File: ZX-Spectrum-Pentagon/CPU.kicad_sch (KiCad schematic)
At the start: 17 parts, among them U2 74HC14, U24 74HC245, U25 74HC541, U26 74HC541, U27 Z80CPU, U28 74HC244, U29 GAL16V8, U30 29F040, U31 74HC32, U8 74HC00

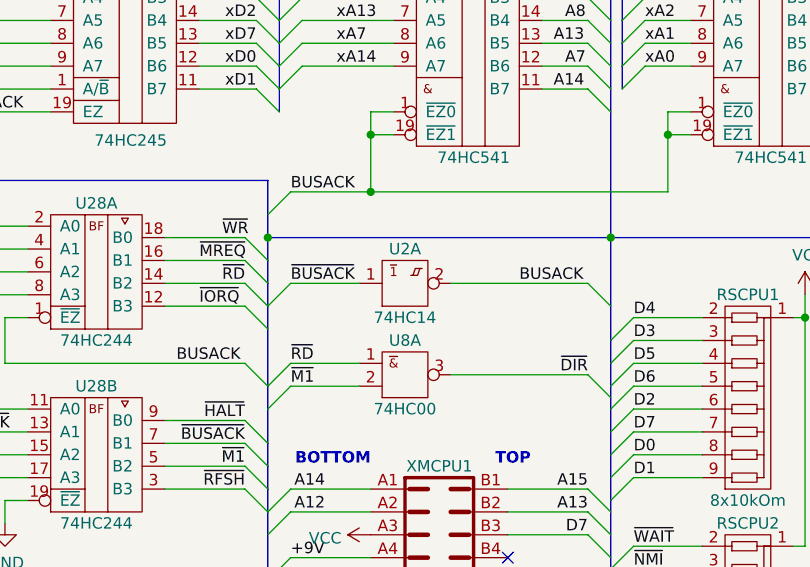
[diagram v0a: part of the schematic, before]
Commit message: delete unuser labels fix problem with units
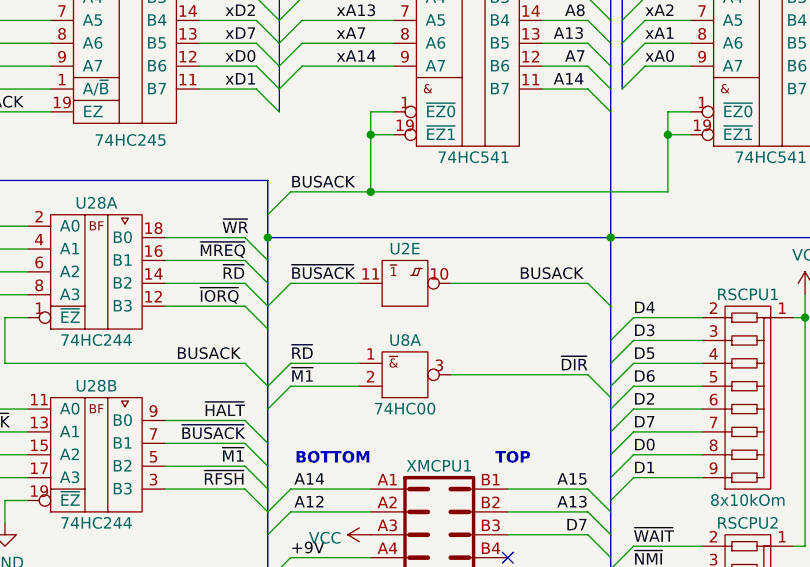
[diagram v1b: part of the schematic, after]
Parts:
- U2: value 74HC14 -> (none); footprint Package_DIP:DIP-14_W7.62mm -> (none)
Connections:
- net BUSACK: now also U2.10 (~{Y}); no longer U2.2 (~{Y})
- net ~{BUSACK}: now also U2.11 (A); no longer U2.1 (A)
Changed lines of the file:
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@@
     (pin "9")
   )
-  (symbol (lib_id "74IEC:74HC14") (at 151.13 67.31 0) (unit 1)
+  (symbol (lib_id "74IEC:74HC14") (at 151.13 67.31 0) (unit 5)
     (in_bom yes) (on_board yes)
     (property "Reference" "U2" (id 0) (at 151.13 63.5 0))
-    (property "Value" "74HC14" (id 1) (at 151.13 71.12 0))
-    (property "Footprint" "Package_DIP:DIP-14_W7.62mm" (id 2) (at 151.13 61.976 0)
+    (property "Value" "" (id 1) (at 151.13 71.12 0))
+    (property "Footprint" "" (id 2) (at 151.13 61.976 0)
       (effects (font (size 1.27 1.27)) hide)
     )

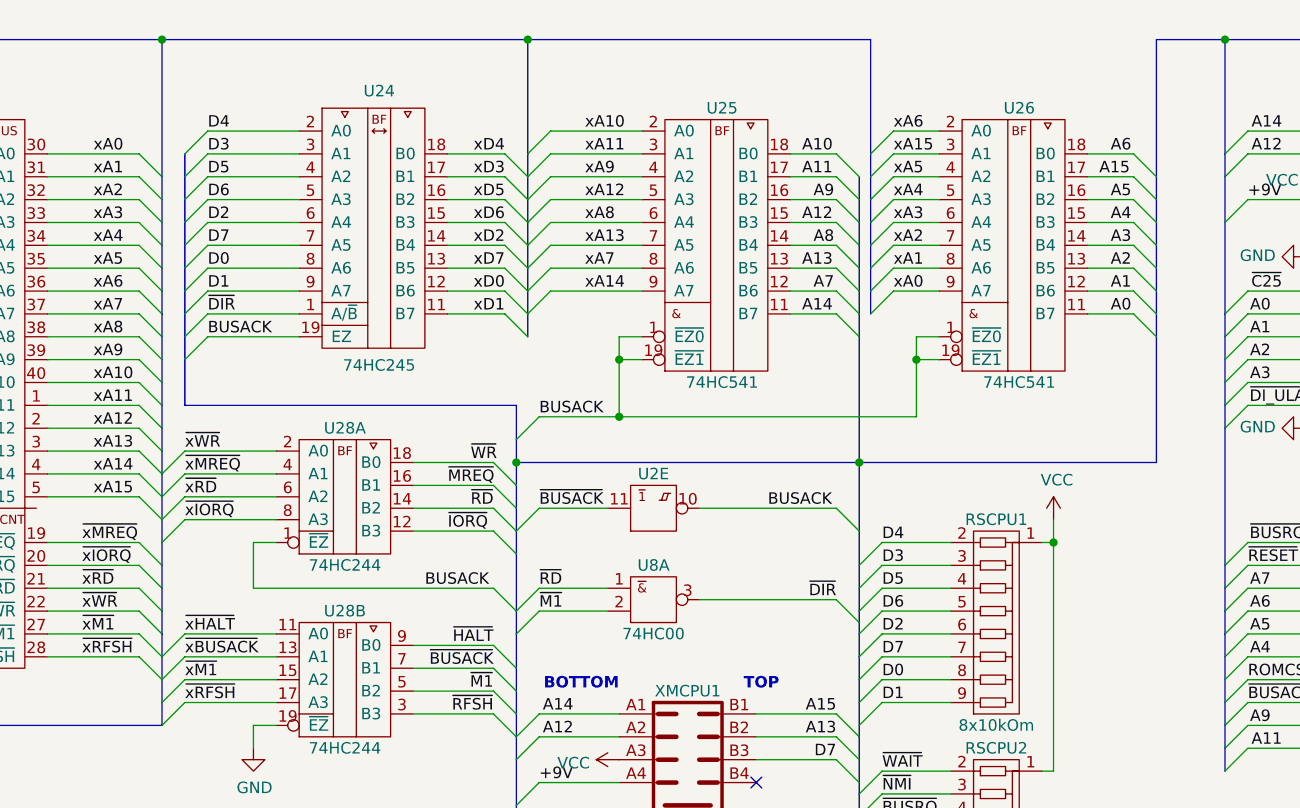
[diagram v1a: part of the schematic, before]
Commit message: chsnge some signals Make a track between CPU and buffers
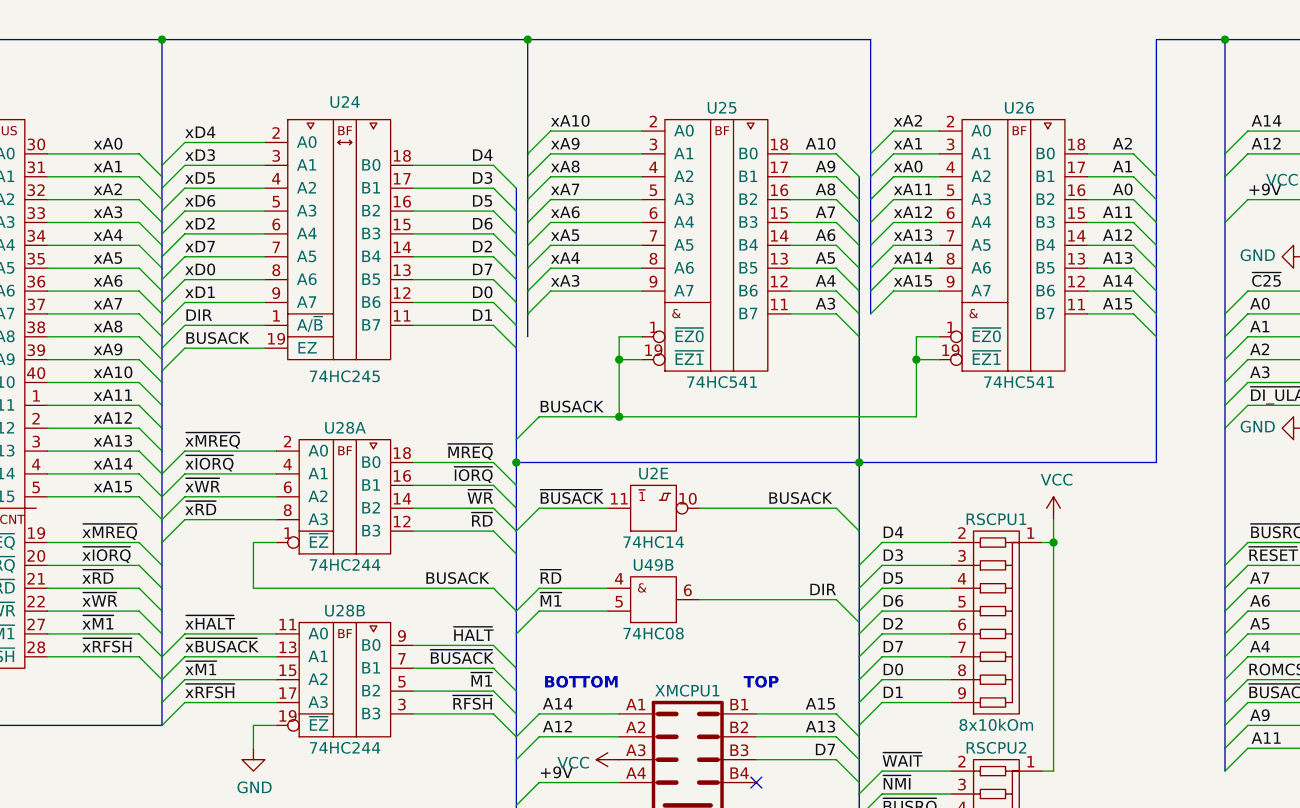
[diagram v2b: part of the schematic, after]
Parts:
- removed U8: 74HC00, Package_DIP:DIP-14_W7.62mm, symbol 74IEC:74HC00
- added U49: 74HC08, symbol 74IEC:74HC08
- U2: value (none) -> 74HC14; footprint (none) -> Package_DIP:DIP-14_W7.62mm
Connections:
- net A0: now also U26.16 (B2); no longer U26.11 (B7)
- net A1: now also U26.17 (B1); no longer U26.12 (B6)
- net A11: now also U26.15 (B3); no longer U25.17 (B1)
- net A12: now also U26.14 (B4); no longer U25.15 (B3)
- net A13: now also U26.13 (B5); no longer U25.13 (B5)
- net A14: now also U26.12 (B6); no longer U25.11 (B7)
- net A15: now also U26.11 (B7); no longer U26.17 (B1)
- net A2: now also U26.18 (B0); no longer U26.13 (B5)
- net A3: now also U25.11 (B7); no longer U26.14 (B4)
- net A4: now also U25.12 (B6); no longer U26.15 (B3)
- net A5: now also U25.13 (B5); no longer U26.16 (B2)
- net A6: now also U25.14 (B4); no longer U26.18 (B0)
- net A7: now also U25.15 (B3); no longer U25.12 (B6)
- net A8: now also U25.16 (B2); no longer U25.14 (B4)
- net A9: now also U25.17 (B1); no longer U25.16 (B2)
- net D0: now also U24.12 (B6); no longer U24.8 (A6)
- net D1: now also U24.11 (B7); no longer U24.9 (A7)
- net D2: now also U24.14 (B4); no longer U24.6 (A4)
- net D3: now also U24.17 (B1); no longer U24.3 (A1)
- net D4: now also U24.18 (B0); no longer U24.2 (A0)
- net D5: now also U24.16 (B2); no longer U24.4 (A2)
- net D6: now also U24.15 (B3); no longer U24.5 (A3)
- net D7: now also U24.13 (B5); no longer U24.7 (A5)
- net GND: now also U49.7 (GND)
- net VCC: now also U49.14 (VCC)
- net xA0: now also U26.4 (A2); no longer U26.9 (A7)
- net xA1: now also U26.3 (A1); no longer U26.8 (A6)
- net xA11: now also U26.5 (A3); no longer U25.3 (A1)
- net xA12: now also U26.6 (A4); no longer U25.5 (A3)
- net xA13: now also U26.7 (A5); no longer U25.7 (A5)
- net xA14: now also U26.8 (A6); no longer U25.9 (A7)
- net xA15: now also U26.9 (A7); no longer U26.3 (A1)
- net xA2: now also U26.2 (A0); no longer U26.7 (A5)
- net xA3: now also U25.9 (A7); no longer U26.6 (A4)
- net xA4: now also U25.8 (A6); no longer U26.5 (A3)
- net xA5: now also U25.7 (A5); no longer U26.4 (A2)
- net xA6: now also U25.6 (A4); no longer U26.2 (A0)
- net xA7: now also U25.5 (A3); no longer U25.8 (A6)
- net xA8: now also U25.4 (A2); no longer U25.6 (A4)
- net xA9: now also U25.3 (A1); no longer U25.4 (A2)
- net xD0: now also U24.8 (A6); no longer U24.12 (B6)
- net xD1: now also U24.9 (A7); no longer U24.11 (B7)
- net xD2: now also U24.6 (A4); no longer U24.14 (B4)
- net xD3: now also U24.3 (A1); no longer U24.17 (B1)
- net xD4: now also U24.2 (A0); no longer U24.18 (B0)
- net xD5: now also U24.4 (A2); no longer U24.16 (B2)
- net xD6: now also U24.5 (A3); no longer U24.15 (B3)
- net xD7: now also U24.7 (A5); no longer U24.13 (B5)
- net ~{IORQ}: now also U28.16 (B1); no longer U28.12 (B3)
- net ~{M1}: now also U49.5 (B)
- net ~{MREQ}: now also U28.18 (B0); no longer U28.16 (B1)
- net ~{RD}: now also U28.12 (B3), U49.4 (A); no longer U28.14 (B2)
- net ~{WR}: now also U28.14 (B2); no longer U28.18 (B0)
- net ~{xIORQ}: now also U28.4 (A1); no longer U28.8 (A3)
- net ~{xMREQ}: now also U28.2 (A0); no longer U28.4 (A1)
- net ~{xRD}: now also U28.8 (A3); no longer U28.6 (A2)
- net ~{xWR}: now also U28.6 (A2); no longer U28.2 (A0)
- net ~{DIR} renamed DIR
- net DIR: now also U49.6 (~{Y})
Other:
- moved on the sheet: U24

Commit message: reposition object
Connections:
- net ~{NMI}: now also RSCPU2.2 (R1); no longer RSCPU2.3 (R2)
- net ~{RST}: now also RSCPU2.3 (R2); no longer RSCPU2.5 (R4)
- net ~{WAIT}: now also RSCPU2.5 (R4); no longer RSCPU2.2 (R1)
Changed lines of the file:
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@@
     (effects (font (size 1.27 1.27)) (justify right bottom))
   )
-  (label "~{NMI}" (at 176.53 99.06 0)
+  (label "~{NMI}" (at 176.53 96.52 0)
     (effects (font (size 1.27 1.27)) (justify left bottom))
   )
@@
     (effects (font (size 1.27 1.27)) (justify left bottom))
   )
-  (label "~{RST}" (at 176.53 104.14 0)
+  (label "~{RST}" (at 176.53 99.06 0)
     (effects (font (size 1.27 1.27)) (justify left bottom))
   )
@@
     (effects (font (size 1.27 1.27)) (justify right bottom))
   )
-  (label "~{WAIT}" (at 176.53 96.52 0)
-    (effects (font (size 1.27 1.27)) (justify left bottom))
-  )
+  (label "~{WAIT}" (at 176.53 104.14 0)
+    (effects (font (size 1.27 1.27)) (justify left bottom))
+  )

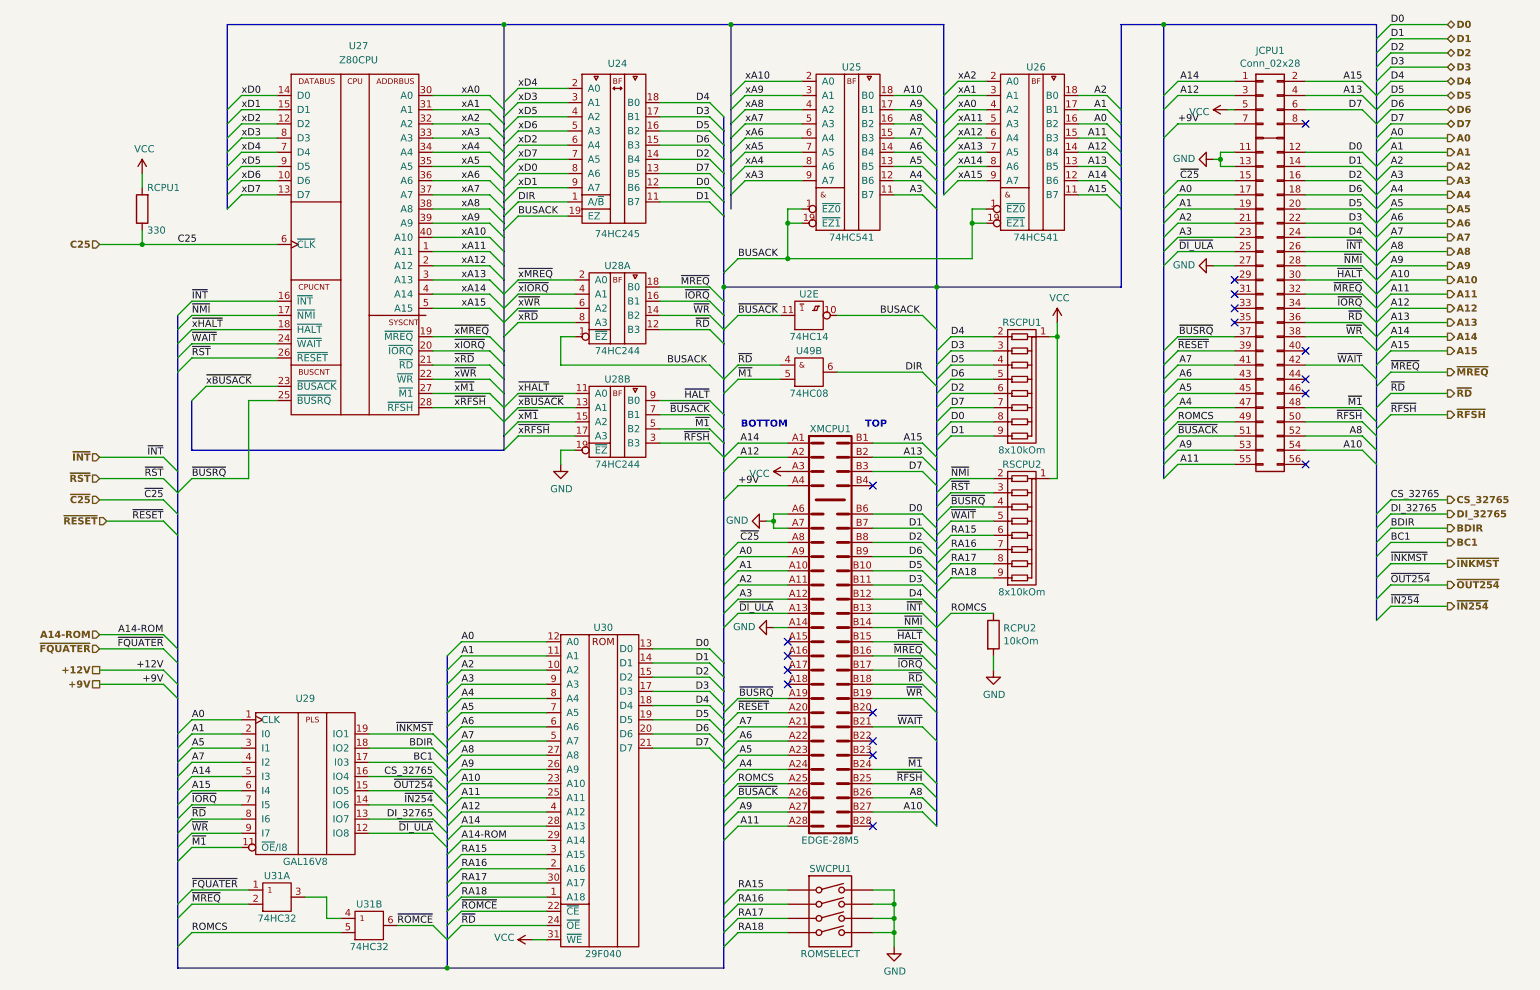
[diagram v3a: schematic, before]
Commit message: rename signals from ROMSC to ~{ROMCS} move resistors
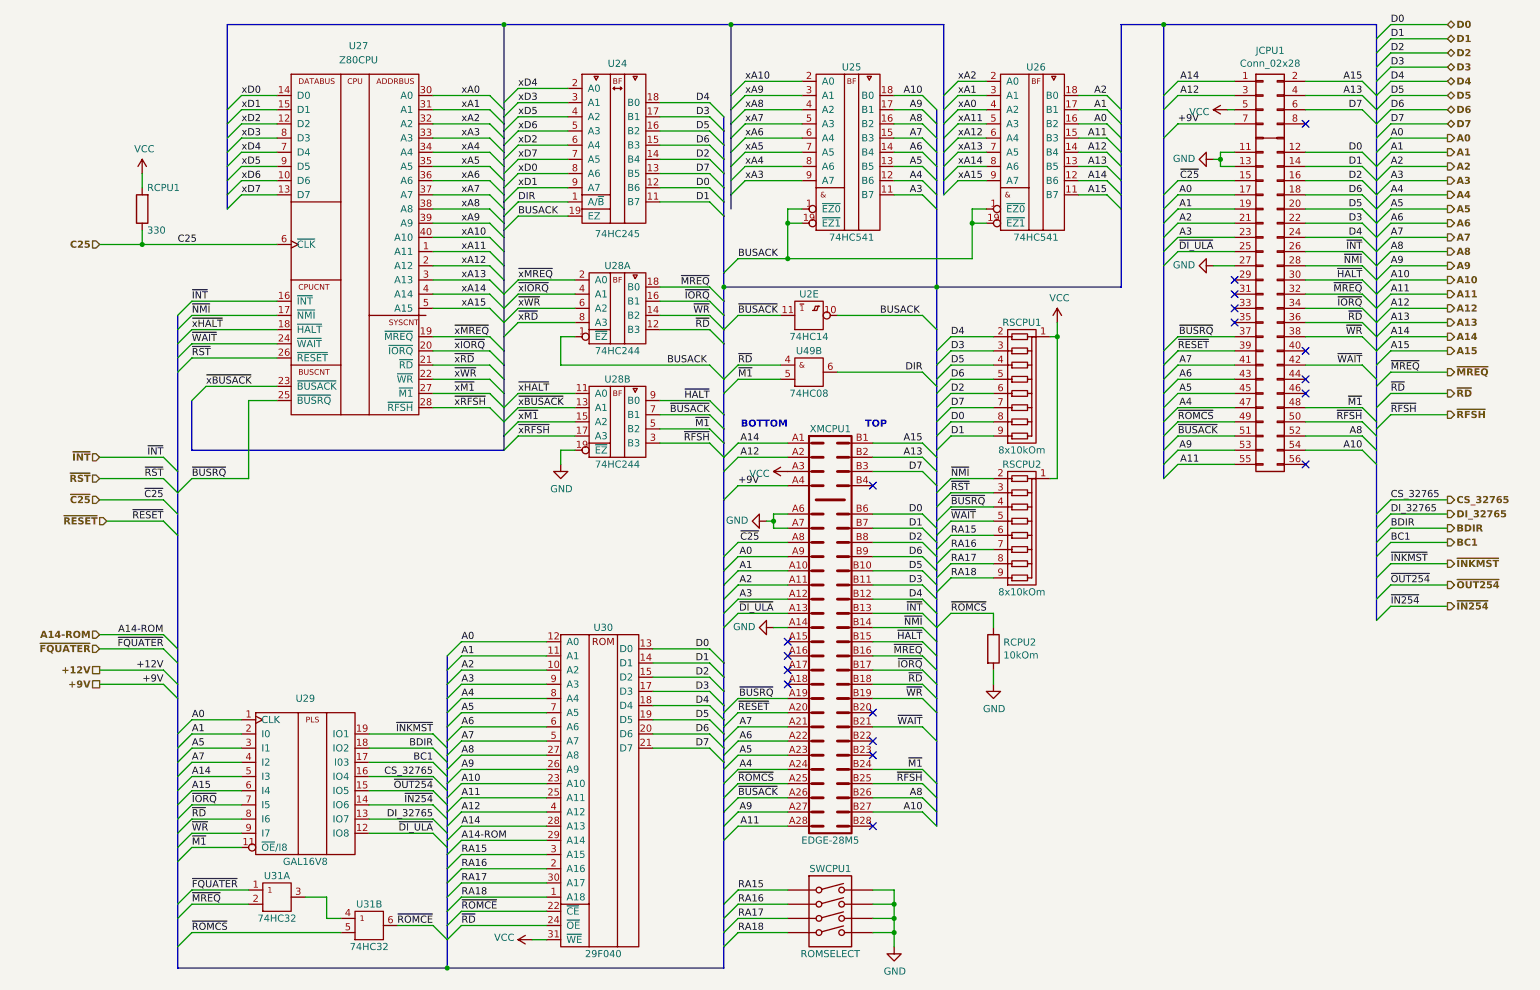
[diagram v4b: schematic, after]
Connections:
- net ROMCS renamed ~{ROMCS}
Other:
- moved on the sheet: RCPU2
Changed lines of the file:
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@@
+    (stroke (width 0) (type default) (color 0 0 0 0))
+  )
+  (wire (pts (xy 184.15 120.65) (xy 184.15 123.19))
     (stroke (width 0) (type default) (color 0 0 0 0))
   )
@@
     (stroke (width 0) (type default) (color 0 0 0 0))
   )
-  (wire (pts (xy 184.15 128.27) (xy 184.15 130.81))
+  (wire (pts (xy 184.15 130.81) (xy 184.15 133.35))
     (stroke (width 0) (type default) (color 0 0 0 0))
   )
@@
     (effects (font (size 1.27 1.27)) (justify right bottom))
   )
-  (label "ROMCS" (at 176.53 120.65 0)
+  (label "~{ROMCS}" (at 176.53 120.65 0)
     (effects (font (size 1.27 1.27)) (justify left bottom))
   )
@@
     (effects (font (size 1.27 1.27)) (justify left bottom))
   )
-  (label "ROMCS" (at 217.17 86.36 0)
+  (label "~{ROMCS}" (at 217.17 86.36 0)
     (effects (font (size 1.27 1.27)) (justify left bottom))
   )
@@
     (effects (font (size 1.27 1.27)) (justify left bottom))
   )
-  (label "ROMCS" (at 138.43 151.13 0)
+  (label "~{ROMCS}" (at 138.43 151.13 0)
     (effects (font (size 1.27 1.27)) (justify left bottom))
   )
@@
     (effects (font (size 1.27 1.27)) (justify left bottom))
   )
-  (label "ROMCS" (at 40.64 177.8 0)
+  (label "~{ROMCS}" (at 40.64 177.8 0)
     (effects (font (size 1.27 1.27)) (justify left bottom))
   )
@@
     (pin "1")
   )
-  (symbol (lib_id "Device:R") (at 184.15 124.46 0) (unit 1)
+  (symbol (lib_id "Device:R") (at 184.15 127 0) (unit 1)
     (in_bom yes) (on_board yes)
-    (property "Reference" "RCPU2" (id 0) (at 185.928 123.2916 0)
+    (property "Reference" "RCPU2" (id 0) (at 185.928 125.8316 0)
       (effects (font (size 1.27 1.27)) (justify left))
     )
-    (property "Value" "10kOm" (id 1) (at 185.928 125.603 0)
+    (property "Value" "10kOm" (id 1) (at 185.928 128.143 0)
       (effects (font (size 1.27 1.27)) (justify left))
     )
-    (property "Footprint" "Resistor_SMD:R_0805_2012Metric_Pad1.20x1.40mm_HandSolder" (id 2) (at 182.372 124.46 90)
-      (effects (font (size 1.27 1.27)) hide)
-    )
-    (property "Datasheet" "~" (id 3) (at 184.15 124.46 0)
+    (property "Footprint" "Resistor_SMD:R_0805_2012Metric_Pad1.20x1.40mm_HandSolder" (id 2) (at 182.372 127 90)
+      (effects (font (size 1.27 1.27)) hide)
+    )
+    (property "Datasheet" "~" (id 3) (at 184.15 127 0)
       (effects (font (size 1.27 1.27)) hide)
     )
@@
     (pin "2")
   )
-  (symbol (lib_id "power:GND") (at 184.15 130.81 0) (unit 1)
+  (symbol (lib_id "power:GND") (at 184.15 133.35 0) (unit 1)
     (in_bom yes) (on_board yes)
-    (property "Reference" "#PWR048" (id 0) (at 184.15 137.16 0)
-      (effects (font (size 1.27 1.27)) hide)
-    )
-    (property "Value" "GND" (id 1) (at 184.277 135.2042 0))
-    (property "Footprint" "" (id 2) (at 184.15 130.81 0)
-      (effects (font (size 1.27 1.27)) hide)
-    )
-    (property "Datasheet" "" (id 3) (at 184.15 130.81 0)
-      (effects (font (size 1.27 1.27)) hide)
-    )
+    (property "Reference" "#PWR048" (id 0) (at 184.15 139.7 0)
+      (effects (font (size 1.27 1.27)) hide)
+    )
+    (property "Value" "GND" (id 1) (at 184.277 137.7442 0))
+    (property "Footprint" "" (id 2) (at 184.15 133.35 0)
+      (effects (font (size 1.27 1.27)) hide)
+    )
+    (property "Datasheet" "" (id 3) (at 184.15 133.35 0)
+      (effects (font (size 1.27 1.27)) hide)
+    )

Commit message: fix address line
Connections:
- net A13: now also U30.28 (A13)
- net A14: no longer U30.28 (A13)
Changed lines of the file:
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@@
     (effects (font (size 1.27 1.27)) (justify left bottom))
   )
-  (label "A14" (at 88.9 158.75 0)
+  (label "A13" (at 88.9 158.75 0)
     (effects (font (size 1.27 1.27)) (justify left bottom))
   )
